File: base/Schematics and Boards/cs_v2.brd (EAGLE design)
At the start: 25.4 x 25.4 mm, 80 parts, among them J101 J-JTAG-CORTEX-NEEDLE6, J301 HIROSE-DF40_44-PIN_CONNECTORS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, J302 HIROSE-DF40_30-PIN_CONNECTORS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, Q201 FK3303010L, Q202 FK3303010L, Q203 FK3303010L, Q204 DMG3415UFY4Q-7, U1 AT25SF641-MHB-T, U101 ATSAMD51, U201 COULOMB-MAX17262, U202 CUS520H3F, U203 MAX77827BEWC+T, U204 SENSOR-SI7006, U205 LOADSWITCH-MIC94164, U206 LOADSWITCH-MIC94164, Y101 16M, Y102 ABS07-32.768KHZ-9-T

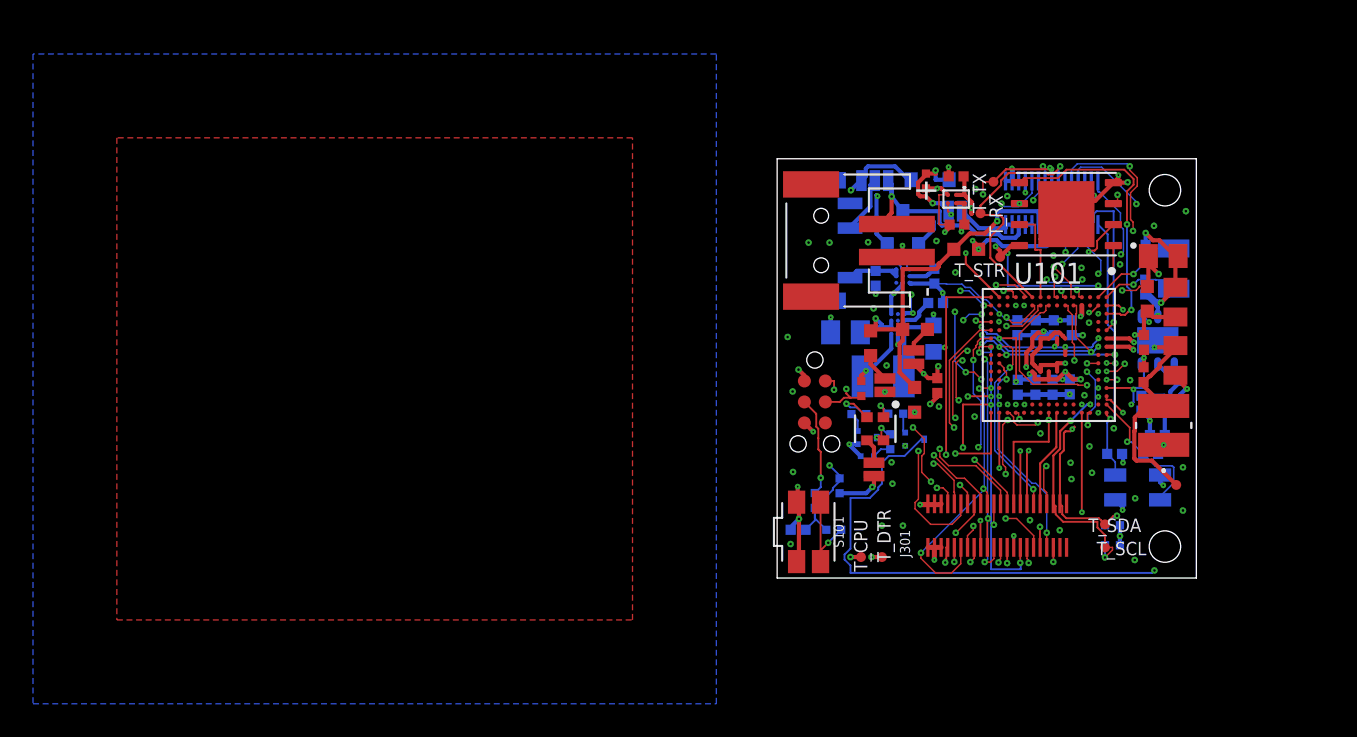
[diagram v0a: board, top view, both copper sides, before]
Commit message: Setup fill polygons
Design complete (until manufacturer points out issues). About 500 vias... ouch
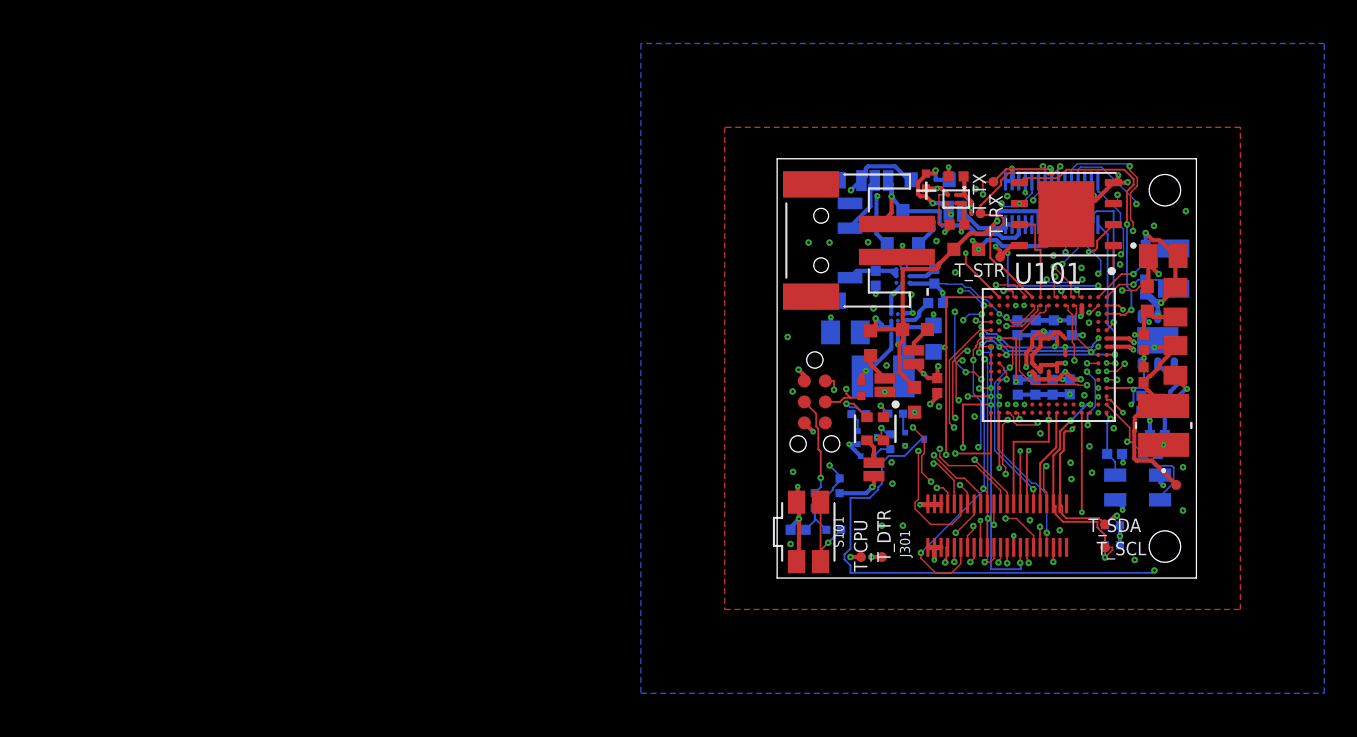
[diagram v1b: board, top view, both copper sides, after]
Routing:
- net GND: vias 116 -> 114
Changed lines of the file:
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@@
 <contactref element="J301" pad="5"/>
 <polygon width="0.254" layer="2">
-<vertex x="-41.275" y="27.94"/>
-<vertex x="-41.275" y="-3.81"/>
-<vertex x="-7.493" y="-3.81"/>
-<vertex x="-7.493" y="27.94"/>
+<vertex x="-4.445" y="28.575"/>
+<vertex x="-4.445" y="-3.175"/>
+<vertex x="29.337" y="-3.175"/>
+<vertex x="29.337" y="28.575"/>
 </polygon>
 <contactref element="S101" pad="2_2"/>
@@
 <contactref element="U1" pad="4"/>
 <polygon width="0.254" layer="16">
-<vertex x="-45.085" y="31.75"/>
-<vertex x="-45.085" y="-7.62"/>
-<vertex x="-3.683" y="-7.62"/>
-<vertex x="-3.683" y="31.75"/>
+<vertex x="-8.255" y="32.385"/>
+<vertex x="-8.255" y="-6.985"/>
+<vertex x="33.147" y="-6.985"/>
+<vertex x="33.147" y="32.385"/>
 </polygon>
 <polygon width="0.254" layer="1">
-<vertex x="-40.005" y="26.67"/>
-<vertex x="-40.005" y="-2.54"/>
-<vertex x="-8.763" y="-2.54"/>
-<vertex x="-8.763" y="26.67"/>
+<vertex x="-3.175" y="27.305"/>
+<vertex x="-3.175" y="-1.905"/>
+<vertex x="28.067" y="-1.905"/>
+<vertex x="28.067" y="27.305"/>
 </polygon>
 <contactref element="J302" pad="1"/>
@@
 <contactref element="J302" pad="5"/>
 <polygon width="0.254" layer="15">
-<vertex x="-43.815" y="-6.35"/>
-<vertex x="-43.815" y="30.48"/>
-<vertex x="-5.08" y="30.48"/>
-<vertex x="-5.08" y="-6.35"/>
+<vertex x="-6.985" y="-5.715"/>
+<vertex x="-6.985" y="31.115"/>
+<vertex x="31.75" y="31.115"/>
+<vertex x="31.75" y="-5.715"/>
 </polygon>
 <via x="14.224" y="24.8158" extent="15-16" drill="0.1016" locked="yes"/>
@@
 <via x="15.3162" y="3.5052" extent="1-16" drill="0.1524"/>
 <via x="21.6662" y="1.0922" extent="1-16" drill="0.1524"/>
-<via x="21.6916" y="4.826" extent="1-16" drill="0.1524"/>
 <via x="20.3962" y="9.0678" extent="1-16" drill="0.1524"/>
 <via x="18.6182" y="11.0744" extent="1-16" drill="0.1524"/>
@@
 <via x="11.684" y="23.0632" extent="2-15" drill="0.1524"/>
 <via x="16.7132" y="16.7386" extent="2-15" drill="0.1524"/>
-<via x="2.1844" y="2.1082" extent="2-15" drill="0.1524"/>
-<wire x1="22.8346" y1="21.336" x2="24.765" y2="22.225" width="0" layer="19" extent="1-1"/>
-<wire x1="22.3266" y1="20.9042" x2="22.8346" y2="21.336" width="0" layer="19" extent="1-1"/>
-<wire x1="8.9916" y1="24.003" x2="9.017" y2="23.6038" width="0" layer="19" extent="1-2"/>
-<wire x1="7.3406" y1="16.2814" x2="7.7152" y2="15.9924" width="0" layer="19" extent="15-16"/>
-<wire x1="9.8044" y1="10.3886" x2="9.271" y2="10.541" width="0" layer="19" extent="1-1"/>
-<wire x1="7.0358" y1="19.9898" x2="7.256" y2="19.447" width="0" layer="19" extent="1-2"/>
-<wire x1="23.8506" y1="16.7132" x2="23.26085" y2="16.6751" width="0" layer="19" extent="1-2"/>
-<wire x1="18.8976" y1="15.4686" x2="18.3859875" y2="15.8459875" width="0" layer="19" extent="1-1"/>
-<wire x1="16.1798" y1="11.5316" x2="16.6878" y2="11.107" width="0" layer="19" extent="15-16"/>
-<wire x1="8.8646" y1="15.8242" x2="8.2296" y2="16.0528" width="0" layer="19" extent="15-15"/>
-<wire x1="9.652" y1="20.4216" x2="10.16" y2="20.955" width="0" layer="19" extent="1-1"/>
-<wire x1="9.4742" y1="19.6088" x2="9.652" y2="20.4216" width="0" layer="19" extent="1-2"/>
-<wire x1="0.8128" y1="2.0574" x2="0.82" y2="2.921" width="0" layer="19" extent="16-16"/>
-<wire x1="18.6182" y1="11.0744" x2="17.7292" y2="11.1324" width="0" layer="19" extent="16-16"/>
-<wire x1="5.842" y1="16.3322" x2="5.969" y2="17.1958" width="0" layer="19" extent="1-15"/>
-<wire x1="6.6294" y1="15.7734" x2="7.3406" y2="16.2814" width="0" layer="19" extent="2-2"/>
-<wire x1="13.9446" y1="23.1394" x2="13.837003125" y2="24.053" width="0" layer="19" extent="16-16"/>
-<wire x1="7.6962" y1="21.4122" x2="8.0137" y2="20.5613" width="0" layer="19" extent="2-2"/>
-<wire x1="21.59" y1="6.35" x2="20.955" y2="6.985" width="0" layer="19" extent="15-15"/>
-<wire x1="9.0678" y1="2.794" x2="9.135003125" y2="1.855" width="0" layer="19" extent="1-2"/>
-<wire x1="0.9652" y1="6.4262" x2="1.2446" y2="5.5372" width="0" layer="19" extent="1-1"/>
-<wire x1="8.5344" y1="19.3802" x2="9.4742" y2="19.6088" width="0" layer="19" extent="2-2"/>
-<wire x1="5.4356" y1="18.5166" x2="5.969" y2="17.711" width="0" layer="19" extent="15-16"/>
-<wire x1="17.2212" y1="10.2616" x2="16.6878" y2="11.107" width="0" layer="19" extent="15-16"/>
-<wire x1="21.6916" y1="4.826" x2="20.9296" y2="4.1148" width="0" layer="19" extent="1-15"/>
-<wire x1="16.7132" y1="16.7386" x2="16.764" y2="15.6138" width="0" layer="19" extent="15-16"/>
-<wire x1="10.287" y1="12.1666" x2="9.7028" y2="11.2086" width="0" layer="19" extent="1-2"/>
-<wire x1="21.3868" y1="11.9888" x2="22.1996" y2="12.769" width="0" layer="19" extent="1-1"/>
-<wire x1="6.985" y1="5.715" x2="6.9342" y2="7.0104" width="0" layer="19" extent="1-1"/>
-<wire x1="11.684" y1="23.0632" x2="10.3458" y2="23.2116" width="0" layer="19" extent="1-2"/>
-<wire x1="12.0142" y1="23.5712" x2="11.684" y2="23.0632" width="0" layer="19" extent="1-2"/>
-<wire x1="2.1844" y1="2.1082" x2="0.8128" y2="2.0574" width="0" layer="19" extent="1-2"/>
-<wire x1="8.6106" y1="6.9088" x2="7.7562" y2="8.0074" width="0" layer="19" extent="15-16"/>
-<wire x1="18.8214" y1="21.463" x2="17.526" y2="22.0472" width="0" layer="19" extent="1-2"/>
-<wire x1="6.858" y1="9.1694" x2="7.14375" y2="7.7851" width="0" layer="19" extent="2-2"/>
-<wire x1="10.795" y1="18.5166" x2="9.525" y2="17.838" width="0" layer="19" extent="16-16"/>
-<wire x1="6.6294" y1="12.8778" x2="7.3152" y2="14.1478" width="0" layer="19" extent="1-15"/>
-<wire x1="24.5872" y1="6.7056" x2="23.2029" y2="6.2364" width="0" layer="19" extent="16-16"/>
-<wire x1="7.62" y1="3.175" x2="9.0678" y2="2.794" width="0" layer="19" extent="1-2"/>
-<wire x1="6.35" y1="3.175" x2="7.62" y2="3.175" width="0" layer="19" extent="1-1"/>
-<wire x1="24.1046" y1="9.4996" x2="22.5878" y2="9.525" width="0" layer="19" extent="15-15"/>
-<wire x1="16.4338" y1="23.1902" x2="17.526" y2="22.0472" width="0" layer="19" extent="1-2"/>
-<wire x1="5.5118" y1="20.3454" x2="7.0358" y2="19.9898" width="0" layer="19" extent="1-2"/>
-<wire x1="20.3962" y1="9.0678" x2="20.897" y2="7.5184" width="0" layer="19" extent="16-16"/>
-<wire x1="17.9832" y1="24.1046" x2="16.4338" y2="23.1902" width="0" layer="19" extent="2-2"/>
-<wire x1="18.923" y1="7.9756" x2="20.3962" y2="9.0678" width="0" layer="19" extent="1-1"/>
-<wire x1="17.78" y1="6.985" x2="18.923" y2="7.9756" width="0" layer="19" extent="1-1"/>
-<wire x1="17.8308" y1="5.9944" x2="17.78" y2="6.985" width="0" layer="19" extent="1-1"/>
-<wire x1="17.8308" y1="5.3594" x2="17.8308" y2="5.9944" width="0" layer="19" extent="1-2"/>
-<wire x1="19.0754" y1="6.3754" x2="17.8308" y2="5.9944" width="0" layer="19" extent="1-1"/>
-<wire x1="17.2466" y1="8.3312" x2="17.78" y2="6.985" width="0" layer="19" extent="1-2"/>
-<wire x1="16.3322" y1="7.8486" x2="17.2466" y2="8.3312" width="0" layer="19" extent="2-2"/>
-<wire x1="15.9512" y1="8.763" x2="16.3322" y2="7.8486" width="0" layer="19" extent="1-2"/>
-<wire x1="15.0368" y1="7.0612" x2="16.3322" y2="7.8486" width="0" layer="19" extent="2-2"/>
-<wire x1="24.5872" y1="4.0894" x2="23.3934" y2="5.6134" width="0" layer="19" extent="1-15"/>
-<wire x1="20.7772" y1="18.9992" x2="22.3266" y2="20.1858" width="0" layer="19" extent="16-16"/>
-<wire x1="0.9398" y1="11.303" x2="1.651" y2="9.398" width="0" layer="19" extent="1-1"/>
-<wire x1="10.6426" y1="8.3312" x2="9.8044" y2="10.3886" width="0" layer="19" extent="1-2"/>
-<wire x1="11.9634" y1="9.779" x2="10.6426" y2="8.3312" width="0" layer="19" extent="1-2"/>
-<wire x1="18.4404" y1="18.796" x2="18.459203125" y2="16.512796875" width="0" layer="19" extent="1-1"/>
-<wire x1="16.7386" y1="19.5326" x2="18.4404" y2="18.796" width="0" layer="19" extent="1-1"/>
-<wire x1="3.175" y1="20.32" x2="5.5118" y2="20.3454" width="0" layer="19" extent="1-1"/>
-<wire x1="1.905" y1="20.32" x2="3.175" y2="20.32" width="0" layer="19" extent="1-1"/>
-<wire x1="14.732" y1="20.9042" x2="13.9446" y2="23.1394" width="0" layer="19" extent="1-2"/>
-<wire x1="4.7244" y1="11.303" x2="6.6294" y2="12.8778" width="0" layer="19" extent="1-2"/>
-<wire x1="17.1196" y1="2.8956" x2="17.8308" y2="5.3594" width="0" layer="19" extent="1-2"/>
-<wire x1="15.3162" y1="3.5052" x2="17.1196" y2="2.8956" width="0" layer="19" extent="1-1"/>
-<wire x1="15.0368" y1="4.3688" x2="15.3162" y2="3.5052" width="0" layer="19" extent="1-2"/>
-<wire x1="14.9606" y1="2.1082" x2="15.3162" y2="3.5052" width="0" layer="19" extent="1-2"/>
-<wire x1="0.635" y1="14.605" x2="3.2402" y2="14.8844" width="0" layer="19" extent="16-16"/>
-<wire x1="6.0706" y1="24.003" x2="8.9916" y2="24.003" width="0" layer="19" extent="2-2"/>
-<wire x1="21.6662" y1="1.0922" x2="20.9296" y2="4.1148" width="0" layer="19" extent="1-15"/>
 </signal>
 <signal name="VDDCORE">
@@
 <signal name="+3V3_PROC">
 <polygon width="0.254" layer="13">
-<vertex x="-42.545" y="-5.08"/>
-<vertex x="-42.545" y="29.21"/>
-<vertex x="-6.35" y="29.21"/>
-<vertex x="-6.35" y="-5.08"/>
+<vertex x="-5.715" y="-4.445"/>
+<vertex x="-5.715" y="29.845"/>
+<vertex x="30.48" y="29.845"/>
+<vertex x="30.48" y="-4.445"/>
 </polygon>
 <contactref element="U101" pad="VDDIO3"/>

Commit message: Renumber parts and remove unneeded silk
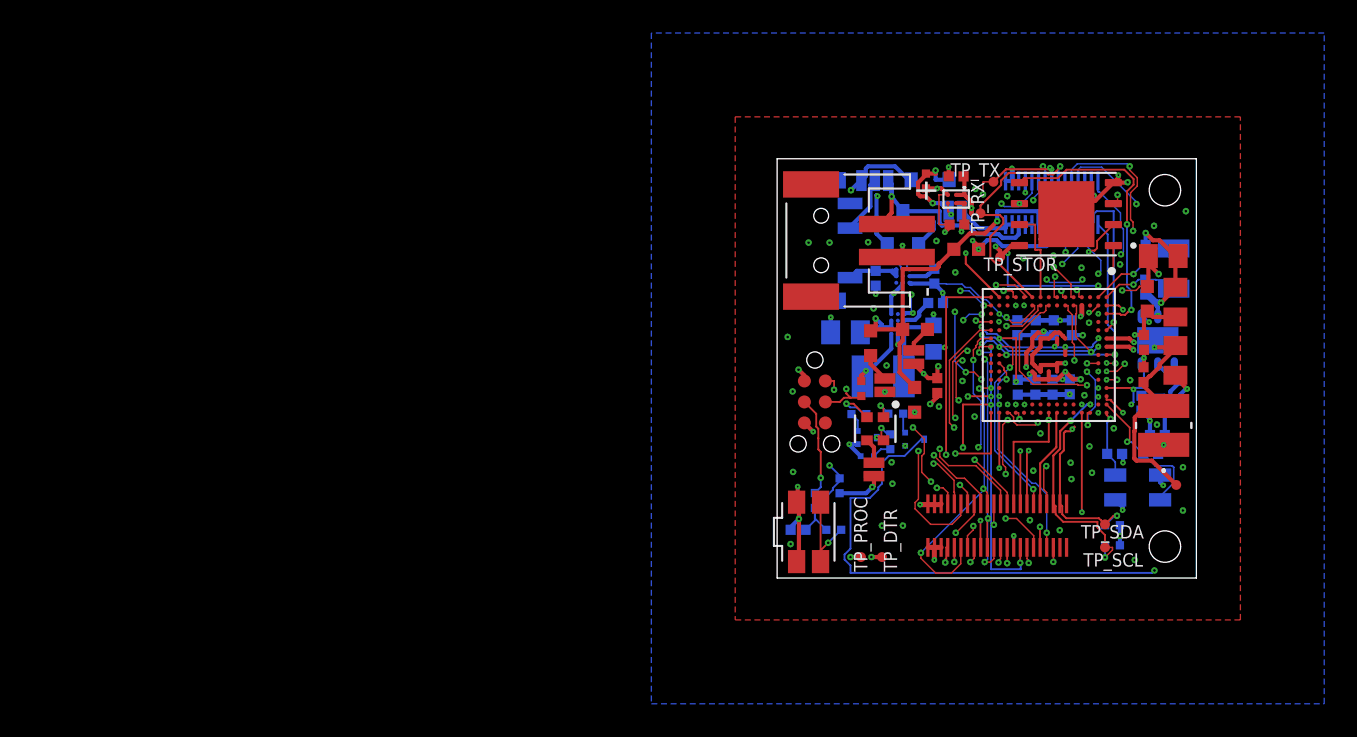
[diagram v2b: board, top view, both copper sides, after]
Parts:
- removed JP_PROC: JUMPER-SMT_2_NC_PASTE_NO-SILK, Connectors:SMT-JUMPER_2_NC_PASTE_NO-SILK
- removed R112: 1k, Resistors:R0402
- removed U206: LOADSWITCH-MIC94164, Switches:WLCSP6_2X3
- added D202: DIALIGHT_RGBLED_598-8710-307FDIALIGHT_598-8710-307F_0_0, Diodes:DIALIGHT_0606_598-8710-307F_0
- added JP205: JUMPER-SMT_2_NC_PASTE_NO-SILK, Connectors:SMT-JUMPER_2_NC_PASTE_NO-SILK
- added R105: 39, Resistors:R0402
- D201: value DIALIGHT_RGBLED_598-8710-307FDIALIGHT_598-8710-307F_0_0 -> CUS520H3F; device Diodes:DIALIGHT_0606_598-8710-307F_0 -> Diodes:CUS520H3F
- Q202: value FK3303010L -> DMG3415UFY4Q-7; device Switches:SSSMINI3 -> Switches:SOT23-3
- Q204: value DMG3415UFY4Q-7 -> FK3303010L; device Switches:SOT23-3 -> Switches:SSSMINI3
- R106: value 39 -> 1k
- R201: value 590 -> 10M
- R203: value 1k -> 590
- R204: value 10M -> 1k
- U202: value CUS520H3F -> MAX77827BEWC+T; device Diodes:CUS520H3F -> Regulators:12-WLP
- U203: value MAX77827BEWC+T -> SENSOR-SI7006; device Regulators:12-WLP -> Sensors:DFN-06
- U204: value SENSOR-SI7006 -> LOADSWITCH-MIC94164; device Sensors:DFN-06 -> Switches:WLCSP6_2X3
- moved U205 17.8 mm to (23.8, 10.8), flipped to the bottom
- moved R204 15.9 mm to (6.86, 8.26), flipped to the bottom, turned to 270 degrees
- moved U203 15.8 mm to (23.1, 14.4), turned to 270 degrees
- moved D201 15.5 mm to (9.27, 24.1), flipped to the bottom, turned to 180 degrees
- moved U204 14.9 mm to (10.8, 23.0), flipped to the top
- moved R201 14.7 mm to (9.02, 24.1), flipped to the top, turned to 90 degrees
- moved Q204 14.6 mm to (5.46, 6.81), turned to 180 degrees
- moved Q202 12.8 mm to (7.62, 21.2), turned to 0 degrees
- moved U202 8.95 mm to (7.32, 15.4), turned to 90 degrees
- moved R106 7.34 mm to (5.11, 11.5), flipped to the top
- moved Q203 3.29 mm to (8.33, 8.41), turned to 90 degrees
- moved JP204 2.44 mm to (8.28, 13.4)
- moved R202 2.24 mm to (4.95, 9.93), turned to 0 degrees
- moved R203 1.73 mm to (7.19, 9.96), turned to 180 degrees
- renumbered JP1 to JP203, JP_VDBG to JP201, T_COR to TP_CPU, T_CPU to TP_PROC, T_DTR to TP_DTR, T_RX to TP_RX, T_SCL to TP_SCL, T_SDA to TP_SDA, T_STR to TP_STOR, T_TMP to TP_TEMP, T_TX to TP_TX, U1 to U102
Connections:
- removed net N$16 (its old number): Q202.2, R202.2
- new net N$17: Q204.2, R204.2
- net +3V3: now also U202.C2, U202.C3; no longer U203.C2, U203.C3
- net +3V3_DTR: now also JP205.1; no longer JP204.1
- net +3V3_DTR_SENSE: now also JP205.2; no longer JP204.2
- net +3V3_PROC: now also JP204.1, R106.2; no longer JP_PROC.1, R112.2
- net +3V3_PROC_SENSE: now also JP204.2; no longer JP_PROC.2
- net +3V3_STOR: now also U204.A1, U204.B1; no longer U205.A1, U205.B1
- net +3V3_STOR_SENSE: now also U204.A2, U204.B2; no longer U205.A2, U205.B2
- net +3V3_TEMP: now also U203.5, U205.A1, U205.B1; no longer U204.5, U206.A1, U206.B1
- net +3V3_TEMP_SENSE: now also U205.A2, U205.B2; no longer U206.A2, U206.B2
- net +3V7_BATT: now also Q202.3; no longer Q204.3
- net DBG_SWCLK: now also R106.1; no longer R112.1
- net DTR_MASTER_I2C_SCL: now also U203.6; no longer U204.6
- net DTR_MASTER_I2C_SDA: now also U203.1; no longer U204.1
- net EN_STOR: now also U204.C2; no longer U205.C2
- net EN_TEMP: now also U205.C2; no longer U206.C2
- net GND: now also Q204.1, R201.1, U202.A4, U202.B1, U202.B2, U203.2, U204.C1; no longer Q202.1, R204.1, U203.A4, U203.B1, U203.B2, U204.2, U206.C1
- net JTAG_NRESET: now also R105.2; no longer R106.2
- net LED_G: now also Q203.3; no longer Q202.3
- net LED_R: now also Q204.3; no longer Q203.3
- net LED_VIN: now also D202.4; no longer D201.4
- net N$12: now also D202.1, R203.1; no longer D201.1, R202.1
- net N$14: now also D202.2, R204.1; no longer D201.2, R203.1
- net N$15: now also R202.2; no longer R201.2
- net N$4: now also D202.3, R202.1; no longer D201.3, R201.1
- net NRESET: now also R105.1; no longer R106.1
- net VDD_DBG_JMP: now also D201.P, Q202.1, R201.2; no longer Q204.1, R204.2, U202.P
- net VDD_SW: now also D201.N, Q202.2; no longer Q204.2, U202.N
- net VREG_BIAS: now also U202.A3; no longer U203.A3
- net VREG_IN: now also U202.A2, U202.C4; no longer U203.A2, U203.C4
- net VREG_LX1: now also U202.A1; no longer U203.A1
- net VREG_LX2: now also U202.C1; no longer U203.C1
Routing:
- net N$16 (its old number): track 1.20 -> 0.00 mm
- net N$17: track 0.00 -> 1.17 mm
- net GND: vias 114 -> 118

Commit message: Generate BOM, CAM files. Submitted to ProtoExpress for custom quote
Expecting to have many updates to do to the board as part of the quote. Expecting cost to be in 4-5k range for a run of 5
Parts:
- L101: value 10u -> L1212; device Inductors:IND_LQH3NPN -> Inductors:L1212
- moved L101 0.40 mm to (23.3, 9.63)
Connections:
- net VDDCORE: now also L101.P$2; no longer L101.2
- net VSW: now also L101.P$1; no longer L101.1
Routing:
- net VDDCORE: track 17.1 -> 16.6 mm
